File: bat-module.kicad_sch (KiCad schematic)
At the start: 33 parts, among them IC1 FDS6898AZ, IC2 DS2777G+, J1 Conn_01x03_Socket

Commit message: general fixes #3 #4
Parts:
- added J2: Conn_01x02_Socket, symbol Connector:Conn_01x02_Socket
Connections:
- net +VBat: now also J2.2 (Pin_2)
- net -VBat: now also J2.1 (Pin_1)
- net VCC: no longer R15.1, R16.1
- new net +3V3: R15.1, R16.1
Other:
- note added: "PICO LOCK CONNECTOR"

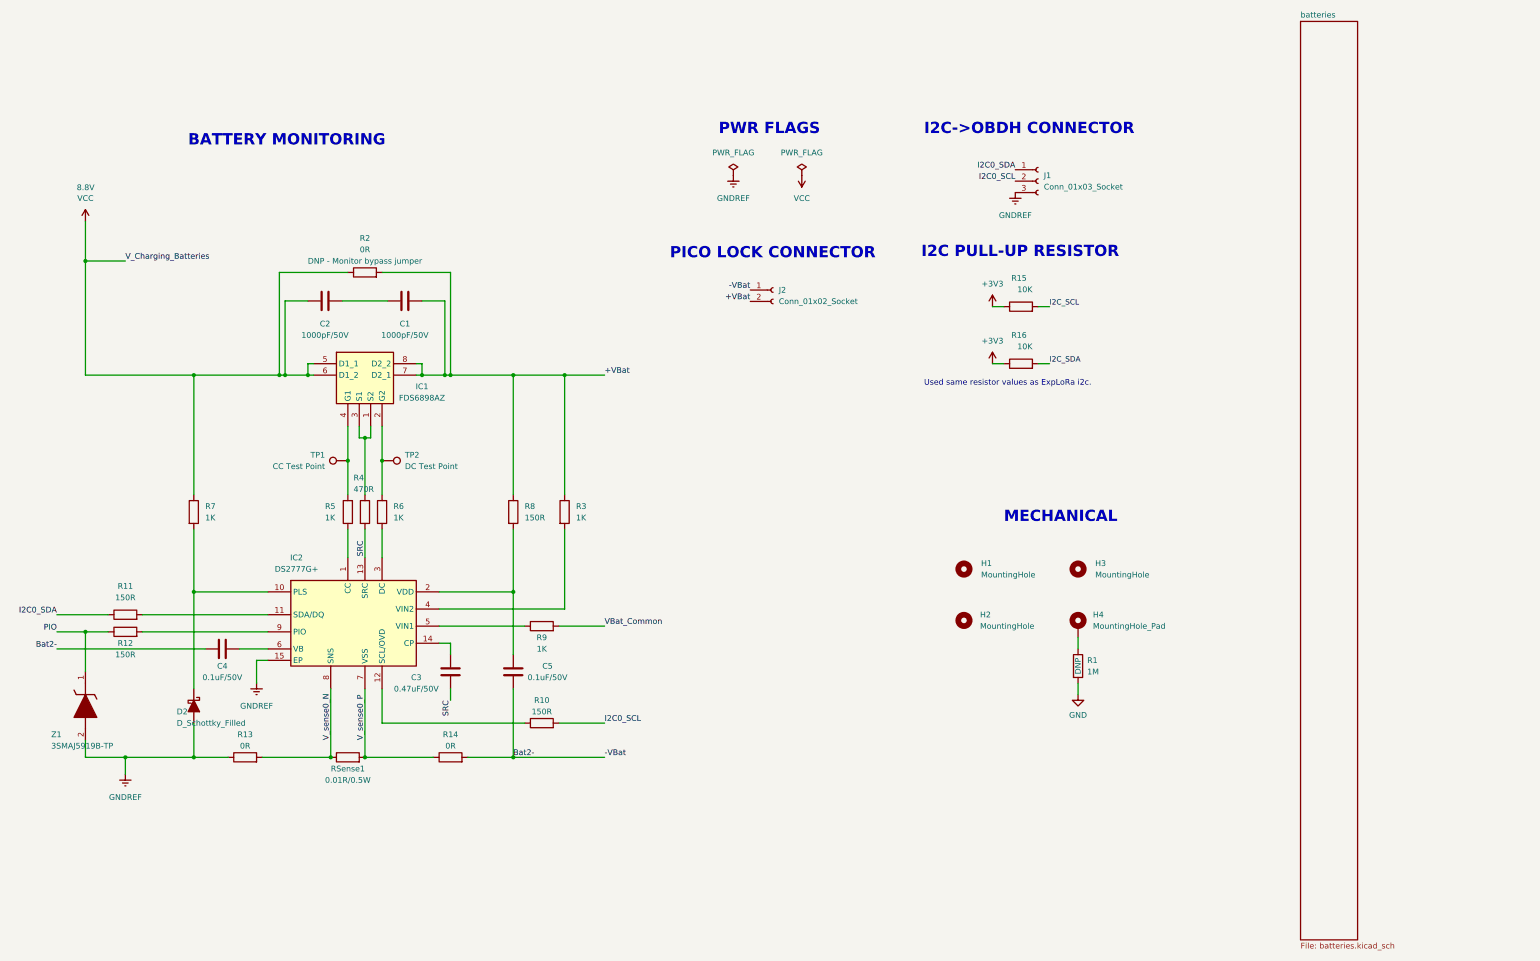
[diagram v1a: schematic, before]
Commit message: developing rtd and heater circuits
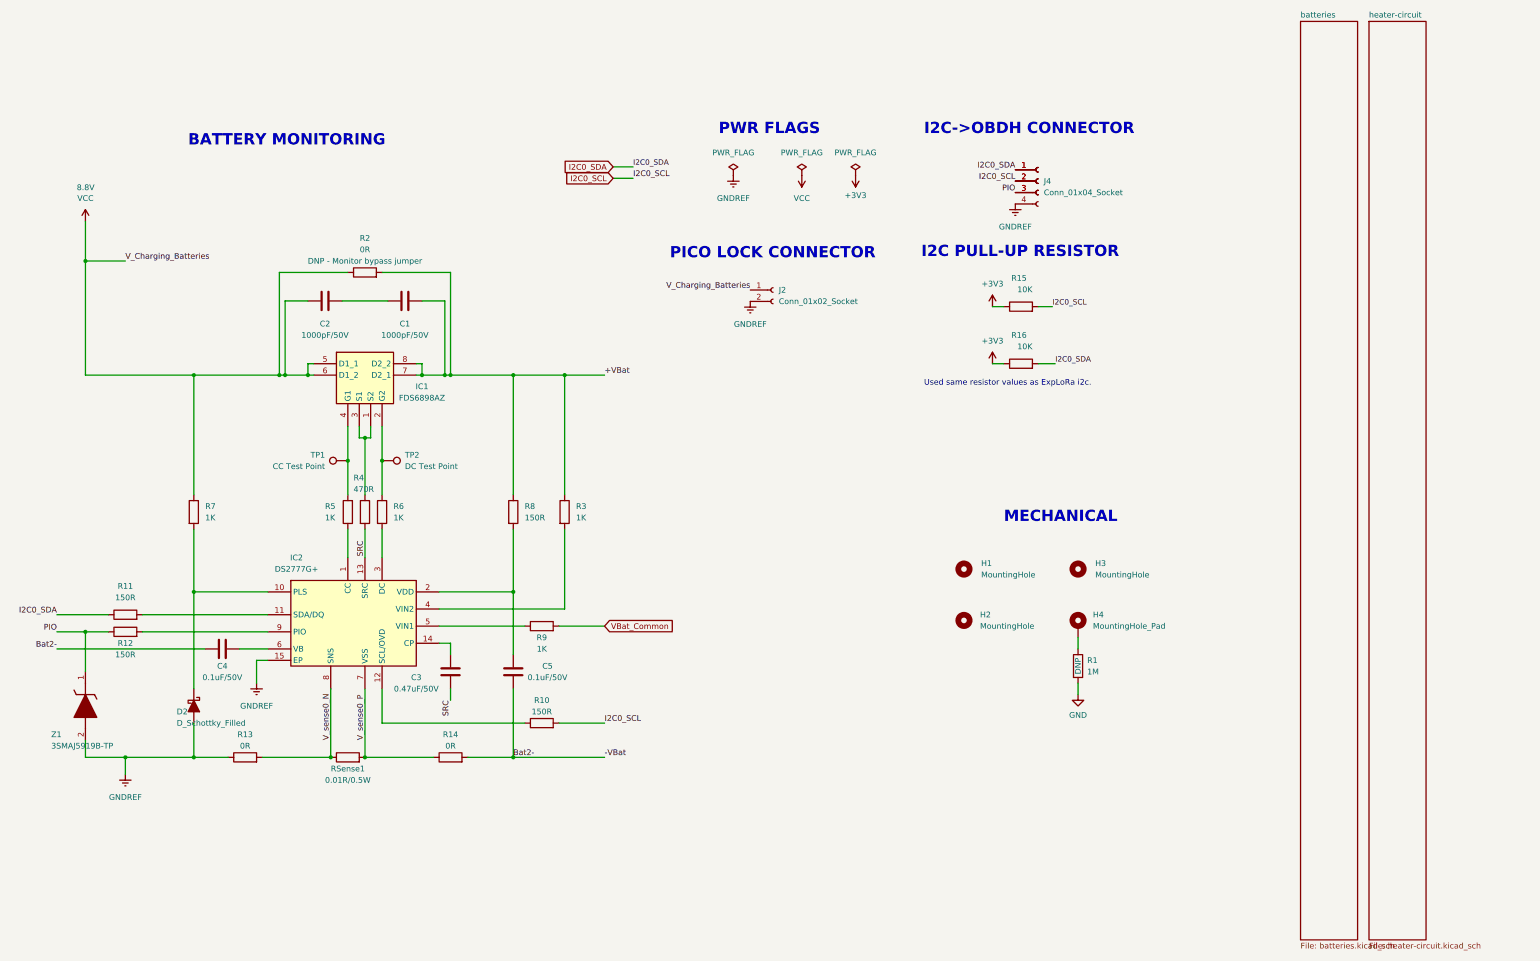
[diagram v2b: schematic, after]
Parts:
- added J4: Conn_01x04_Socket, symbol Connector:Conn_01x04_Socket
- C1, C2, C3, C4, C5: footprint (none) -> Capacitor_SMD:C_0603_1608Metric_Pad1.08x0.95mm_HandSolder
- IC1: footprint (none) -> lib:FDS6898AZ
- IC2: footprint (none) -> lib:DS2777G+
- R10, R11, R12, R13, R14, R2, R3, R4, R5, R6, R7, R8, R9: footprint (none) -> Resistor_SMD:R_0603_1608Metric_Pad0.98x0.95mm_HandSolder
- Z1: footprint (none) -> DIOM5226X244N
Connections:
- net I2C_SCL is gone; now on net I2C0_SCL: R15.2
- net I2C_SDA is gone; now on net I2C0_SDA: R16.2
- net +VBat: no longer J2.2 (Pin_2)
- net -VBat: no longer J2.1 (Pin_1)
- net GNDREF: now also J2.2 (Pin_2), J4.4 (Pin_4); no longer J1.3 (Pin_3)
- net I2C0_SCL: now also J4.2 (Pin_2)
- net I2C0_SDA: now also J4.1 (Pin_1)
- net PIO: now also J1.3 (Pin_3), J4.3 (Pin_3)
- net VCC: now also J2.1 (Pin_1)
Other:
- added sheet heater-circuit (heater-circuit.kicad_sch)

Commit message: fixing voltages and uploading heater circuit
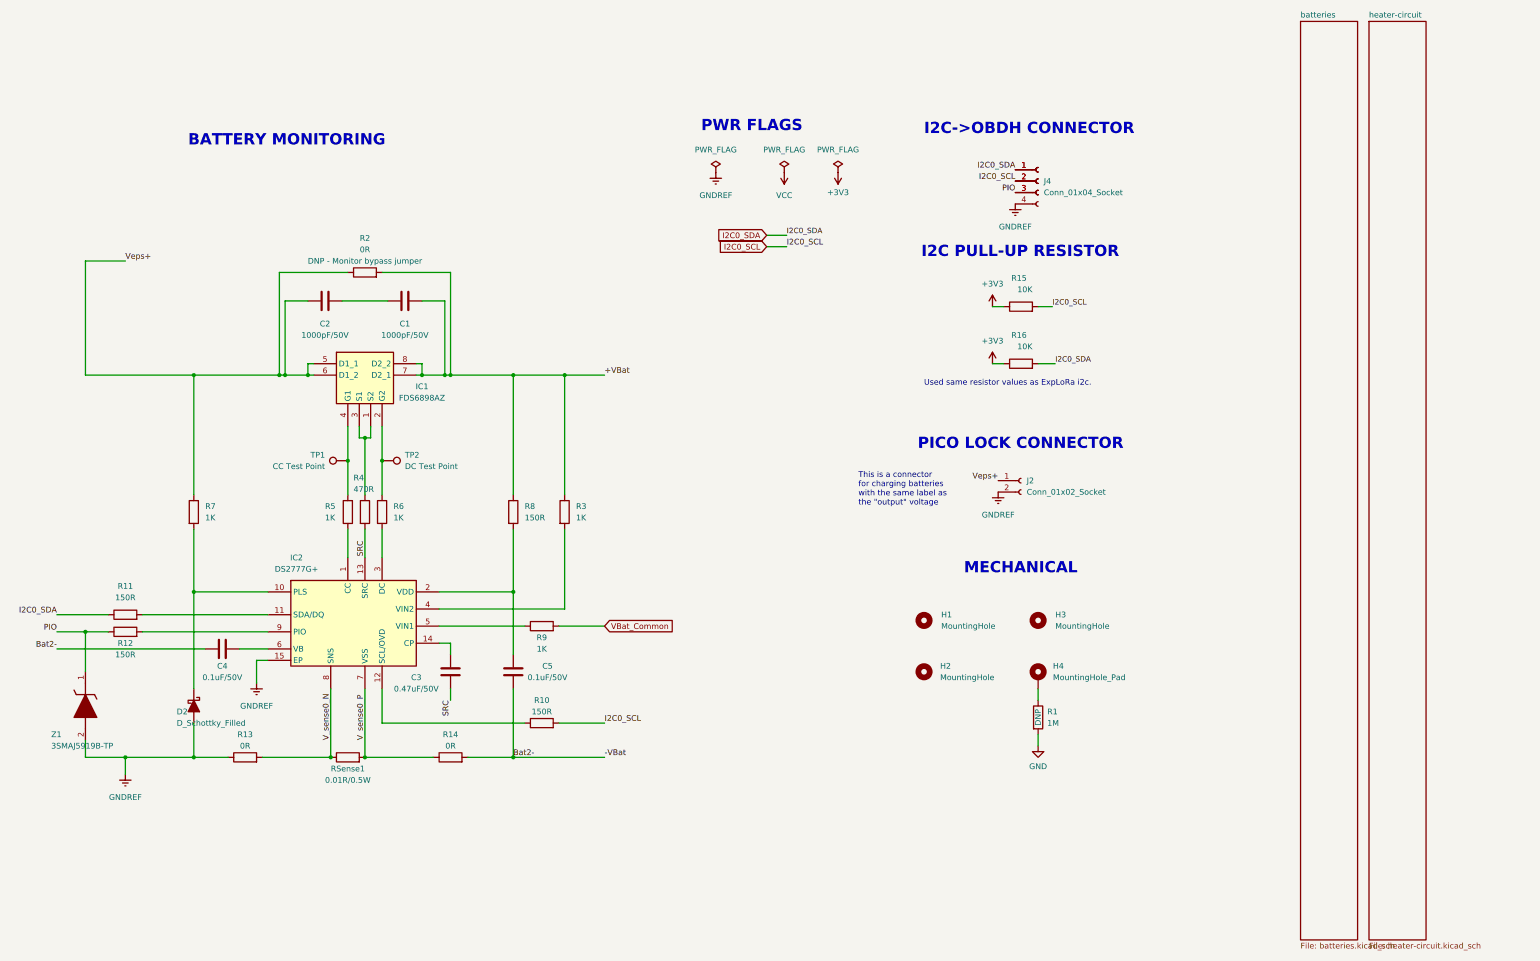
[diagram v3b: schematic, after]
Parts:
- J1, J4: footprint (none) -> Connector_Molex:Molex_PicoBlade_53048-0410_1x04_P1.25mm_Horizontal
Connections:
- net VCC: no longer C2.2, IC1.5 (D1_1), IC1.6 (D1_2), J2.1 (Pin_1), R2.1, R7.1
- new net Veps+: C2.2, IC1.5 (D1_1), IC1.6 (D1_2), J2.1 (Pin_1), R2.1, R7.1
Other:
- note added: "This is a connector for charging batteries with the same label as the "output" voltage"
- moved on the sheet: H1, H2, H3, H4, J2, R1

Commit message: Creating hierarquical labels and organizing root
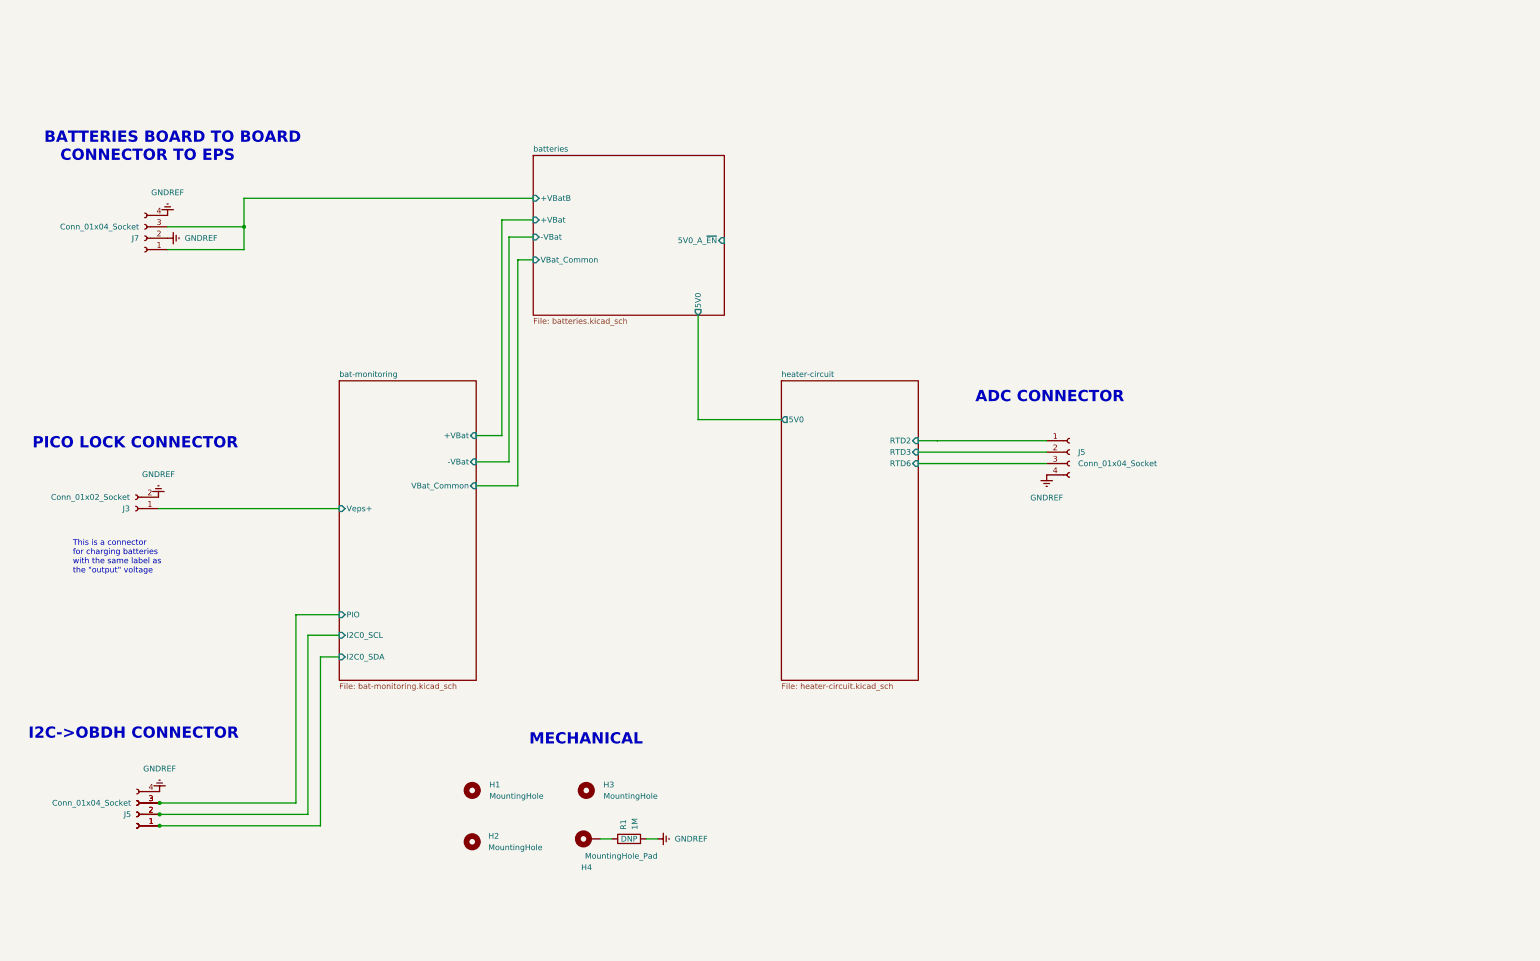
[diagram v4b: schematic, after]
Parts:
- removed C1, C2: 1000pF/50V, Capacitor_SMD:C_0603_1608Metric_Pad1.08x0.95mm_HandSolder, symbol Device:C
- removed C3: 0.47uF/50V, Capacitor_SMD:C_0603_1608Metric_Pad1.08x0.95mm_HandSolder, symbol Device:C
- removed C4, C5: 0.1uF/50V, Capacitor_SMD:C_0603_1608Metric_Pad1.08x0.95mm_HandSolder, symbol Device:C
- removed D2: D_Schottky_Filled, symbol Device:D_Schottky_Filled
- removed IC1: FDS6898AZ, lib:FDS6898AZ, symbol FDS6898AZ-:FDS6898AZ
- removed IC2: DS2777G+, lib:DS2777G+, symbol DS2777G+:DS2777G+
- removed J1: Conn_01x03_Socket, Connector_Molex:Molex_PicoBlade_53048-0410_1x04_P1.25mm_Horizontal, symbol Connector:Conn_01x03_Socket
- removed J2: Conn_01x02_Socket, symbol Connector:Conn_01x02_Socket
- removed J4: Conn_01x04_Socket, Connector_Molex:Molex_PicoBlade_53048-0410_1x04_P1.25mm_Horizontal, symbol Connector:Conn_01x04_Socket
- removed R10, R11, R12, R8: 150R, Resistor_SMD:R_0603_1608Metric_Pad0.98x0.95mm_HandSolder, symbol Device:R
- removed R13, R14, R2: 0R, Resistor_SMD:R_0603_1608Metric_Pad0.98x0.95mm_HandSolder, symbol Device:R
- removed R15, R16: 10K, Resistor_SMD:R_0603_1608Metric_Pad0.98x0.95mm_HandSolder, symbol Device:R
- removed R3, R5, R6, R7, R9: 1K, Resistor_SMD:R_0603_1608Metric_Pad0.98x0.95mm_HandSolder, symbol Device:R
- removed R4: 470R, Resistor_SMD:R_0603_1608Metric_Pad0.98x0.95mm_HandSolder, symbol Device:R
- removed RSense1: 0.01R/0.5W, symbol Device:R
- removed TP1: CC Test Point, symbol Connector:TestPoint
- removed TP2: DC Test Point, symbol Connector:TestPoint
- removed Z1: 3SMAJ5919B-TP, DIOM5226X244N, symbol 3SMAJ5919B-TP:3SMAJ5919B-TP
- added J3: Conn_01x02_Socket, symbol Connector:Conn_01x02_Socket
- added J4: Conn_01x03_Socket, Connector_Molex:Molex_PicoBlade_53048-0410_1x04_P1.25mm_Horizontal, symbol Connector:Conn_01x03_Socket
- added J5, J7: Conn_01x04_Socket, symbol Connector:Conn_01x04_Socket
- added J5: Conn_01x04_Socket, Connector_Molex:Molex_PicoBlade_53048-0410_1x04_P1.25mm_Horizontal, symbol Connector:Conn_01x04_Socket
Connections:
- net GND is gone; now on net GNDREF: R1.2
- net GNDREF: now also J3.2 (Pin_2), J5.4 (Pin_4), J5.4 (Pin_4), J7.2 (Pin_2), J7.4 (Pin_4)
- new net bat-monitoring/I2C0_SCL: J4.2 (Pin_2), J5.2 (Pin_2)
- new net bat-monitoring/I2C0_SDA: J4.1 (Pin_1), J5.1 (Pin_1)
- new net bat-monitoring/PIO: J4.3 (Pin_3), J5.3 (Pin_3)
- new net bat-monitoring/Veps+: J3.1 (Pin_1)
- new net batteries/+VBatB: J7.1 (Pin_1), J7.3 (Pin_3)
- new net heater-circuit/RTD2: J5.1 (Pin_1)
- new net heater-circuit/RTD3: J5.2 (Pin_2)
- new net heater-circuit/RTD6: J5.3 (Pin_3)
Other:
- added sheet bat-monitoring (bat-monitoring.kicad_sch)
- sheet batteries ports: added +VBat, +VBatB, -VBat, 5V0, 5V0_A_~{EN}, VBat_Common; removed none
- sheet heater-circuit ports: added 5V0, RTD2, RTD3, RTD6; removed none
- note added: "ADC CONNECTOR"
- note added: "BATTERIES BOARD TO BOARD CONNECTOR TO EPS"
- note removed: "BATTERY MONITORING"
- note removed: "I2C PULL-UP RESISTOR"
- note removed: "PWR FLAGS"
- note removed: "Used same resistor values as ExpLoRa i2c."
